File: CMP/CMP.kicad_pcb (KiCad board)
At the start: 2 copper layers, 81.3 x 40.6 mm, 12 parts, among them J1 Conn_01x04_Male, J2 Conn_01x08_Male, J3 Conn_01x08_Male, J4 Conn_01x08_Male, J5 Conn_01x03_Male, J6 Conn_01x03_Male, J7 Conn_01x01_Male, U1 74LS85, U2 74HC4078, U3 74LS85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

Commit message: CMP cmd is ready
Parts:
- added R1: 10k, Resistor_SMD:R_0805_2012Metric_Pad1.20x1.40mm_HandSolder, F.Cu at (133.3, 75.6)
- moved U4 17.8 mm to (86.4, 52.1), turned to 0 degrees
- moved U5 17.8 mm to (68.6, 52.1), turned to 0 degrees
- moved J5 10.2 mm to (134.0, 58.4)
- moved J6 10.2 mm to (134.0, 48.3)
- moved U2 5.24 mm to (113.0, 68.6), turned to 0 degrees
- moved J7 2.62 mm to (134.0, 68.6)
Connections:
- J5 pad 1: /GT -> /LT
- J5 pad 2: /LT -> /EQ
- J5 pad 3: /EQ -> /GT
- J6 pad 1: /GT_IN -> /EQ_IN
- J6 pad 3: /EQ_IN -> /GT_IN
- U2 pad 10: /O3 -> /O5
- U2 pad 11: /O4 -> /O6
- U2 pad 12: /O5 -> /O7
- U2 pad 2: /O7 -> /O0
- U2 pad 3: /O6 -> /O1
- U2 pad 4: /O1 -> /O2
- U2 pad 5: /O0 -> /O3
- U2 pad 9: /O2 -> /O4
- U4 pad 1: /GT_IN -> GND
- U4 pad 11: Net-(U4-Pad11) -> /LT(I)
- U4 pad 12: Net-(U4-Pad12) -> /Expand
- U4 pad 13: Net-(U4-Pad13) -> /LT_IN
- U4 pad 2: /Expand -> GND
- U4 pad 3: /GT(I) -> Net-(U4-Pad3)
- U4 pad 4: Net-(U4-Pad4) -> GND
- U4 pad 5: Net-(U4-Pad5) -> GND
- U4 pad 8: /EQ(I) -> /GT(I)
- U4 pad 9: Net-(U4-Pad9) -> /GT_IN
- U5 pad 1: /EQ_IN -> GND
- U5 pad 11: Net-(U5-Pad11) -> Net-(U5-Pad10)
- U5 pad 12: Net-(U5-Pad12) -> /EQ_IN
- U5 pad 13: Net-(U5-Pad13) -> /EQ_IN
- U5 pad 2: /EQ_IN -> GND
- U5 pad 3: Net-(U4-Pad9) -> Net-(U5-Pad3)
- U5 pad 4: /LT_IN -> GND
- U5 pad 5: /Expand -> GND
- U5 pad 6: /LT(I) -> Net-(U5-Pad6)
- U5 pad 8: Net-(U5-Pad8) -> /EQ(I)
- U5 pad 9: Net-(U5-Pad9) -> /Expand
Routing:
- net VCC: track 0.00 -> 202.4 mm
- net GND: track 0.00 -> 138.4 mm, vias 0 -> 4
- net /Expand: track 0.00 -> 106.7 mm
- net /EQ_IN: track 0.00 -> 75.2 mm
- net /LT: track 0.00 -> 53.2 mm
- net /EQ: track 0.00 -> 50.8 mm
- net /GT: track 0.00 -> 49.7 mm
- net /A7: track 0.00 -> 46.0 mm
- net /LT_IN: track 0.00 -> 45.7 mm
- net /GT_IN: track 0.00 -> 45.7 mm
- net Net-(U1-Pad2): track 0.00 -> 30.1 mm
- net /B3: track 0.00 -> 29.7 mm, vias 0 -> 1
- net /ZF: track 0.00 -> 28.2 mm
- net Net-(U1-Pad3): track 0.00 -> 27.0 mm
- net /B1: track 0.00 -> 26.5 mm
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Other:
- board size 81.3 x 40.6 mm -> 81.3 x 37.1 mm
- net class Default: trace_width 0.25 -> 0.5; via_dia 0.8 -> 1.5; via_drill 0.4 -> 0.5

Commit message: Polishing CMP
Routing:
- net /EQ: track 50.8 -> 52.7 mm
- net /GT: track 49.7 -> 51.1 mm
- net /LT: track 53.2 -> 54.2 mm
- net /LT(I): track 25.1 -> 25.7 mm
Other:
- board text added: "EQ"
- board text added: "EQ_IN"
- board text added: "GT"
- board text added: "GT_IN"
- board text added: "LT"
- board text added: "LT_IN"
- board text added: "Vcc"
- board text added: "ZF"

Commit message: Polishing CMP
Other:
- board text added: "0"
- board text added: "7"
- board text added: "DST(A)"
- board text added: "Expand"
- board text added: "Gnd"
- board text added: "OUT"
- board text added: "SRC(B)"
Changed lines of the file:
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@@
   (general
     (thickness 1.6)
-    (drawings 17)
+    (drawings 29)
     (tracks 360)
     (zones 0)
@@
     (tags "resistor handsolder")
     (attr smd)
-    (fp_text reference R1 (at 3.175 0) (layer F.SilkS)
+    (fp_text reference R1 (at 0 1.905) (layer F.SilkS)
       (effects (font (size 1 1) (thickness 0.15)))
     )
@@
     )
   )
+  (gr_text Expand (at 135.89 74.295 90) (layer F.SilkS)
+    (effects (font (size 1 1) (thickness 0.15)))
+  )
+  (gr_text Gnd (at 130.81 75.565 90) (layer F.SilkS)
+    (effects (font (size 1 1) (thickness 0.15)))
+  )
+  (gr_text Vcc (at 128.27 75.565 90) (layer F.SilkS)
+    (effects (font (size 1 1) (thickness 0.15)))
+  )
+  (gr_text "DST(A)" (at 67.31 75.565) (layer F.SilkS)
+    (effects (font (size 1.5 1.5) (thickness 0.2)))
+  )
+  (gr_text "SRC(B)" (at 89.535 75.565) (layer F.SilkS)
+    (effects (font (size 1.5 1.5) (thickness 0.2)))
+  )
+  (gr_text OUT (at 113.03 75.565) (layer F.SilkS)
+    (effects (font (size 1.5 1.5) (thickness 0.2)))
+  )
+  (gr_text 7 (at 121.92 76.2) (layer F.SilkS)
+    (effects (font (size 1 1) (thickness 0.15)))
+  )
+  (gr_text 0 (at 104.14 76.2) (layer F.SilkS)
+    (effects (font (size 1 1) (thickness 0.15)))
+  )
+  (gr_text 7 (at 99.06 76.2) (layer F.SilkS)
+    (effects (font (size 1 1) (thickness 0.15)))
+  )
+  (gr_text 0 (at 81.28 76.2) (layer F.SilkS)
+    (effects (font (size 1 1) (thickness 0.15)))
+  )
+  (gr_text 7 (at 76.2 76.2) (layer F.SilkS)
+    (effects (font (size 1 1) (thickness 0.15)))
+  )
+  (gr_text 0 (at 58.42 76.2) (layer F.SilkS)
+    (effects (font (size 1 1) (thickness 0.15)))
+  )
   (gr_text Vcc (at 128.27 75.565 90) (layer F.Cu)

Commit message: Print settings? Photo mask
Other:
- board text added: "28.11.2022"
- board text added: "74HCPU"
- board text added: "CMP"

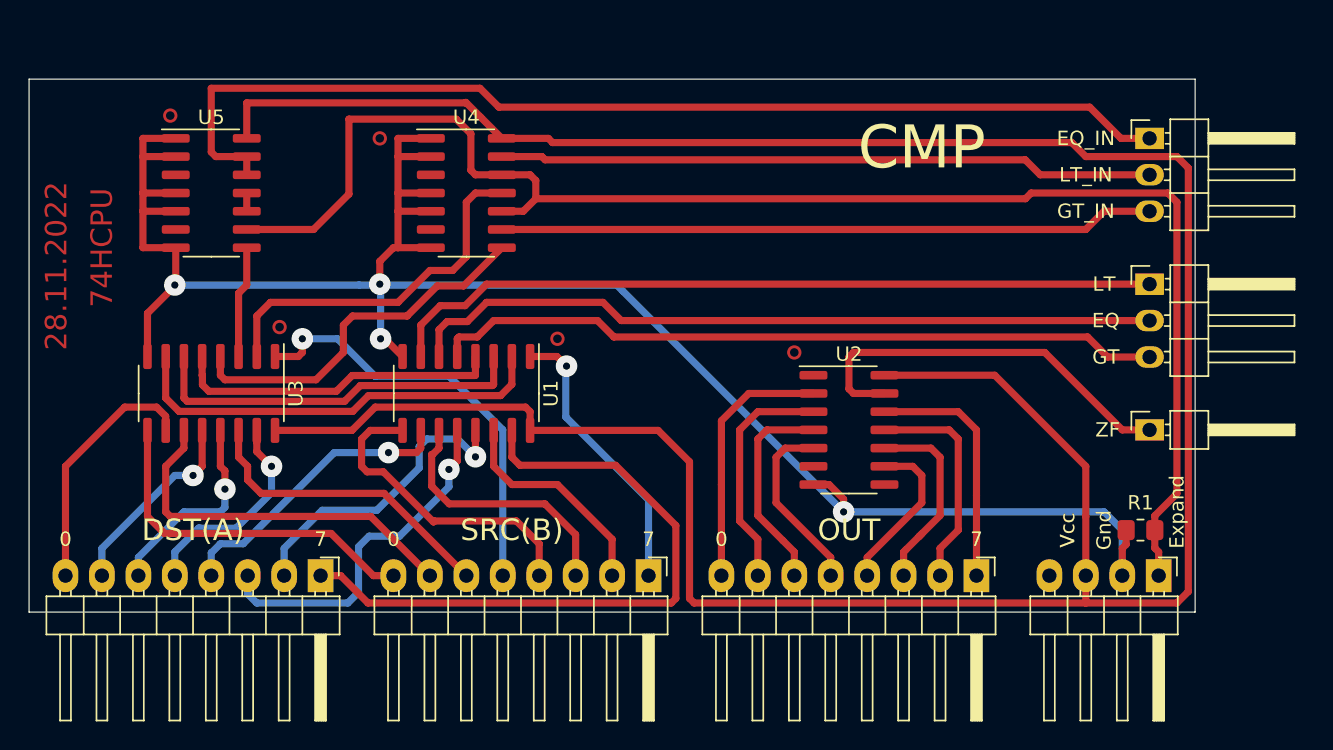
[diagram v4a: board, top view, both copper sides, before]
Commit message: Add lost invertor and caps
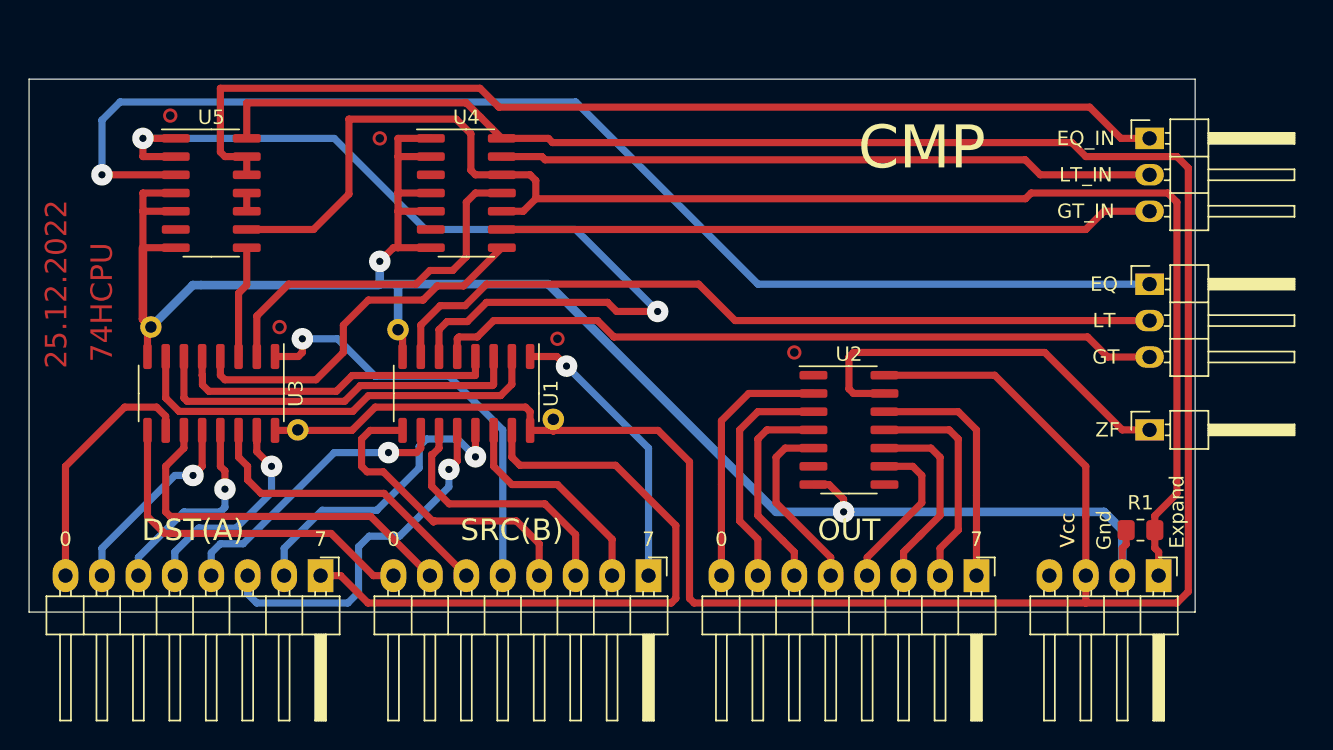
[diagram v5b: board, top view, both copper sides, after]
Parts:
- added C1: 0.1uF, Capacitor_THT:C_Axial_L3.8mm_D2.6mm_P12.50mm_Horizontal, B.Cu at (74.6, 68.6)
- added C2: 0.1uF, Capacitor_THT:C_Axial_L3.8mm_D2.6mm_P12.50mm_Horizontal, B.Cu at (92.4, 67.8)
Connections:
- J5 pad 1: /LT -> /EQ
- J5 pad 2: /EQ -> /LT
- U1 pad 6: /EQ -> Net-(U1-Pad6)
- U5 pad 1: GND -> Net-(U1-Pad6)
- U5 pad 2: GND -> Net-(U1-Pad6)
- U5 pad 3: Net-(U5-Pad3) -> /EQ
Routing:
- net Net-(U1-Pad6): track 0.00 -> 64.9 mm, vias 0 -> 2
- net /EQ: track 52.7 -> 87.8 mm, vias 0 -> 1
- net GND: track 138.4 -> 131.9 mm, vias 4 -> 2
- net /EQ_IN: track 75.2 -> 73.9 mm
- net /LT: track 54.2 -> 55.2 mm
- net VCC: track 202.4 -> 203.2 mm
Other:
- board text added: "25.12.2022"
- board text removed: "28.11.2022"
